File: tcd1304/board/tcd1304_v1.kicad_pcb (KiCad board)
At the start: 2 copper layers, 53.3 x 48.2 mm, 29 parts, among them Q1 MMBT3906LT1G, U1 SN74AC14NSR

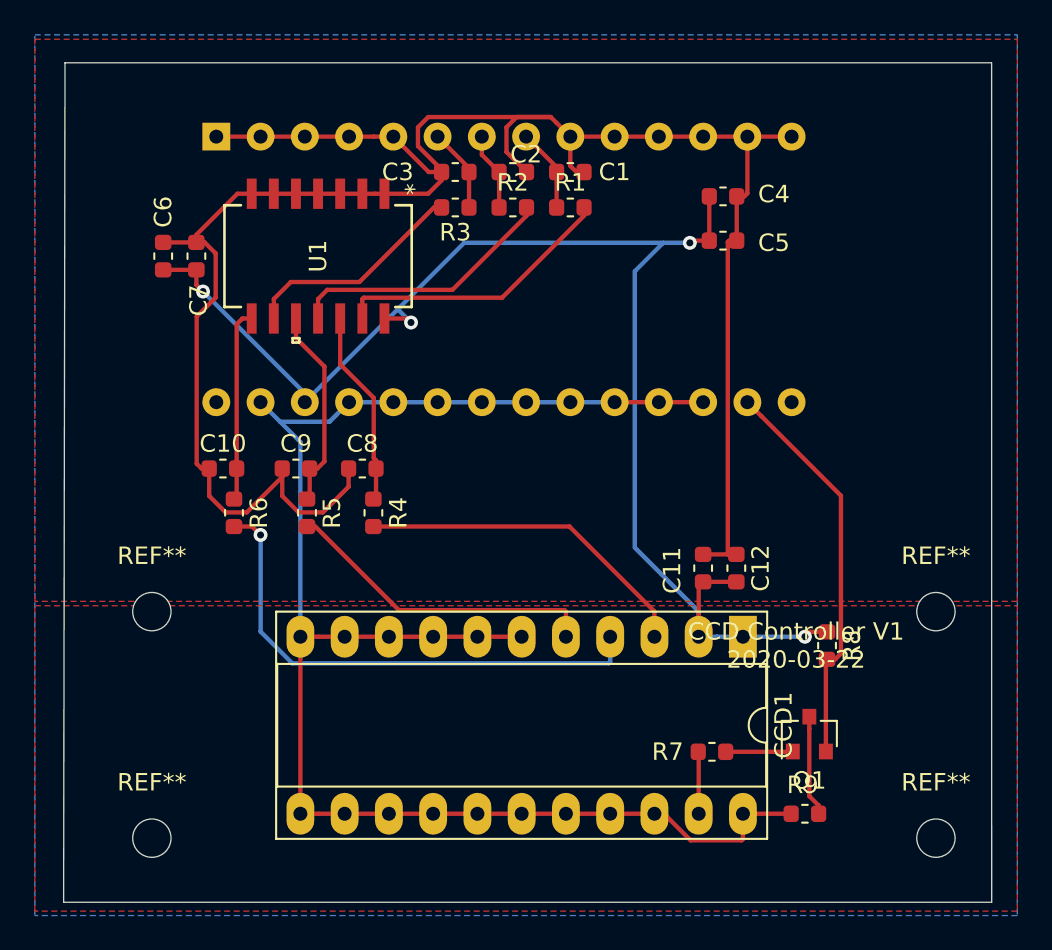
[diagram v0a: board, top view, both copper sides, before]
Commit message: New version for the PCB (updated silk screen)
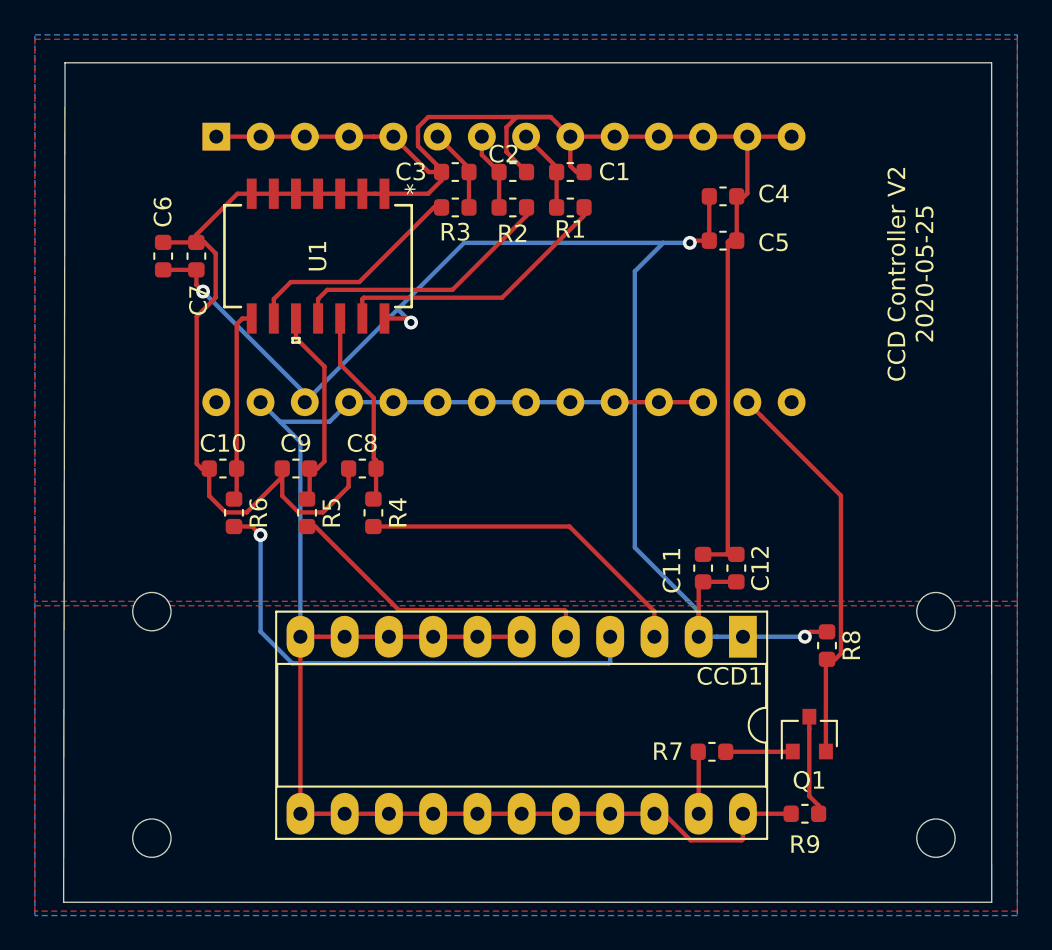
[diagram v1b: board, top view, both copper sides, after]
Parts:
- removed REF** (x3): MountingHole_2.2mm_M2, MountingHole:MountingHole_2.2mm_M2
- added  : MountingHole_2.2mm_M2, MountingHole:MountingHole_2.2mm_M2, F.Cu at (120.0, 90.0)
- added  : MountingHole_2.2mm_M2, MountingHole:MountingHole_2.2mm_M2, F.Cu at (120.0, 103.0)
- added  : MountingHole_2.2mm_M2, MountingHole:MountingHole_2.2mm_M2, F.Cu at (165.0, 90.0)
-  : renamed from REF**
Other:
- board text added: "CCD Controller V2 2020-05-25"
- board text removed: "CCD Controller V1 2020-03-22"
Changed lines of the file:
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@@
     (tags "mounting hole 2.2mm no annular m2")
     (attr virtual)
-    (fp_text reference REF** (at 0 -3.2) (layer F.SilkS)
+    (fp_text reference " " (at 0 -3.2) (layer F.SilkS)
       (effects (font (size 1 1) (thickness 0.15)))
     )
@@
     (tags "mounting hole 2.2mm no annular m2")
     (attr virtual)
-    (fp_text reference REF** (at 0 -3.2) (layer F.SilkS)
+    (fp_text reference " " (at 0 -3.2) (layer F.SilkS)
       (effects (font (size 1 1) (thickness 0.15)))
     )
@@
     (tags "mounting hole 2.2mm no annular m2")
     (attr virtual)
-    (fp_text reference REF** (at 0 -3.2) (layer F.SilkS)
+    (fp_text reference " " (at 0 -3.2) (layer F.SilkS)
       (effects (font (size 1 1) (thickness 0.15)))
     )
@@
     (tags "mounting hole 2.2mm no annular m2")
     (attr virtual)
-    (fp_text reference REF** (at 0 -3.2) (layer F.SilkS)
+    (fp_text reference " " (at 0 -3.2) (layer F.SilkS)
       (effects (font (size 1 1) (thickness 0.15)))
     )
@@
     (descr "22-lead though-hole mounted DIP package, row spacing 10.16 mm (400 mils), Socket, LongPads")
     (tags "THT DIP DIL PDIP 2.54mm 10.16mm 400mil Socket LongPads")
-    (fp_text reference CCD1 (at 5.08 -2.33 90) (layer F.SilkS)
+    (fp_text reference CCD1 (at 2.286 0.762 180) (layer F.SilkS)
       (effects (font (size 1 1) (thickness 0.15)))
     )
@@
     (tags resistor)
     (attr smd)
-    (fp_text reference R2 (at 0 -1.43) (layer F.SilkS)
+    (fp_text reference R2 (at 0 1.524) (layer F.SilkS)
       (effects (font (size 1 1) (thickness 0.15)))
     )
@@
     (tags resistor)
     (attr smd)
-    (fp_text reference R1 (at 0 -1.43) (layer F.SilkS)
+    (fp_text reference R1 (at 0 1.27) (layer F.SilkS)
       (effects (font (size 1 1) (thickness 0.15)))
     )
@@
     (tags capacitor)
     (attr smd)
-    (fp_text reference C3 (at 3.302 0) (layer F.SilkS)
+    (fp_text reference C3 (at 2.54 0) (layer F.SilkS)
       (effects (font (size 1 1) (thickness 0.15)))
     )
@@
     (tags capacitor)
     (attr smd)
-    (fp_text reference C2 (at 0.762 -1.016) (layer F.SilkS)
+    (fp_text reference C2 (at -0.508 -1.016) (layer F.SilkS)
       (effects (font (size 1 1) (thickness 0.15)))
     )
@@
     (tags resistor)
     (attr smd)
-    (fp_text reference R9 (at 0.127 1.651) (layer F.SilkS)
+    (fp_text reference R9 (at 0 -1.778) (layer F.SilkS)
       (effects (font (size 1 1) (thickness 0.15)))
     )
@@
     )
   )
-  (gr_text "CCD Controller V1\n2020-03-22" (at 156.972 91.948) (layer F.SilkS)
+  (gr_text "CCD Controller V2\n2020-05-25" (at 163.576 70.612 90) (layer F.SilkS)
     (effects (font (size 1 1) (thickness 0.15)))
   )
